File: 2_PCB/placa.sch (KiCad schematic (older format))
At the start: 35 parts

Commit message: Updated some sensor values; Finished choice of components; Placements of components in PCB
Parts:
- removed C? (x2): 100n, symbol Device:C
- added C13: 660n, Capacitor_SMD:C_0805_2012Metric_Pad1.15x1.40mm_HandSolder, symbol Device:C
- added C15: 100n, Capacitor_SMD:C_0805_2012Metric_Pad1.15x1.40mm_HandSolder, symbol Device:C
- added C16: 470n, Capacitor_SMD:C_0805_2012Metric_Pad1.15x1.40mm_HandSolder, symbol Device:C
- added J1: Screw_Terminal_01x02, Connector_PinHeader_2.54mm:PinHeader_1x02_P2.54mm_Vertical, symbol Connector:Screw_Terminal_01x02
- added JP1: SolderJumper_3_Bridged12, Jumper:SolderJumper-3_P1.3mm_Bridged12_RoundedPad1.0x1.5mm_NumberLabels, symbol Jumper:SolderJumper_3_Bridged12
- C1, C3, C8: renamed from C?; footprint (none) -> Capacitor_SMD:C_0805_2012Metric_Pad1.15x1.40mm_HandSolder
- C10: renamed from C?; value CP1 -> 660n; footprint (none) -> Capacitor_SMD:C_0805_2012Metric_Pad1.15x1.40mm_HandSolder
- C11, C14: renamed from C?; value C_Small -> 10p; footprint (none) -> Capacitor_SMD:C_0805_2012Metric_Pad1.15x1.40mm_HandSolder
- C2: renamed from C?; value C -> 100n; footprint (none) -> Capacitor_SMD:C_0805_2012Metric_Pad1.15x1.40mm_HandSolder
- C4: renamed from C?; value CP1 -> 10u; footprint (none) -> Capacitor_THT:CP_Radial_D5.0mm_P2.50mm
- C5: renamed from C?; value CP1 -> 1u; footprint (none) -> Capacitor_THT:CP_Radial_D5.0mm_P2.00mm
- C6, C9: renamed from C?; value C_Small -> 20p; footprint (none) -> Capacitor_SMD:C_0805_2012Metric_Pad1.15x1.40mm_HandSolder
- C7: renamed from C?; value 100n -> 660n; footprint (none) -> Capacitor_SMD:C_0805_2012Metric_Pad1.15x1.40mm_HandSolder
- D1, D2: renamed from D?; footprint (none) -> LED_SMD:LED_0805_2012Metric_Pad1.15x1.40mm_HandSolder
- J2: renamed from J?; footprint (none) -> Connector_PinHeader_2.54mm:PinHeader_1x05_P2.54mm_Vertical
- J3: renamed from J?; footprint (none) -> Connector_PinHeader_2.54mm:PinHeader_1x02_P2.54mm_Vertical
- R1, R10, R4, R6, R9: renamed from R?; footprint (none) -> Resistor_SMD:R_0805_2012Metric_Pad1.15x1.40mm_HandSolder
- R2, R3: renamed from R?; value R -> 330; footprint (none) -> Resistor_SMD:R_0805_2012Metric_Pad1.15x1.40mm_HandSolder
- R5: renamed from R?; value R -> 390; footprint (none) -> Resistor_SMD:R_0805_2012Metric_Pad1.15x1.40mm_HandSolder
- R7: renamed from R?; value R -> 10k; footprint (none) -> Resistor_SMD:R_0805_2012Metric_Pad1.15x1.40mm_HandSolder
- R8: renamed from R?; value R_Variable -> HR202; footprint (none) -> Resistor_THT:R_Box_L8.4mm_W2.5mm_P5.08mm
- SW1: renamed from SW?; footprint (none) -> TCC:BUTTON_5mm
- TH1: renamed from TH?; footprint (none) -> Resistor_THT:R_Axial_DIN0204_L3.6mm_D1.6mm_P1.90mm_Vertical
- Y1: renamed from Y?; value Crystal_Small -> 8 MHz; footprint (none) -> Crystal:Crystal_HC49-U_Vertical
- Y2: renamed from Y?; value Crystal_Small -> 32.768 kHz; footprint (none) -> Crystal:Crystal_Round_D1.0mm_Vertical
- gave numbers to parts that had none: 3
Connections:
- net labels added: PWR_MS, PWR_RH, PWR_TEMP, UART_RX, UART_TX
- net labels removed: VDDA
- wire segments 156 -> 177
- no-connect marks 8 -> 24
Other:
- note added: "LoRa RA-01"
- note added: "Microcontroller"
- note added: "UART Connection"
- moved on the sheet: C11, C14, C2, C3, C4, C6, C7, C9, D1, D2, R1, R2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

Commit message: Remap SPI pins, reposition components; start routing
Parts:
- added J4: TestPoints, Connector_PinHeader_2.54mm:PinHeader_1x04_P2.54mm_Vertical, symbol Connector:Conn_01x04_Female
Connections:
- wire segments 177 -> 181
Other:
- moved on the sheet: C16, C3, C4
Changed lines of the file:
@@
 Text Notes 6000 650  0    50   ~ 0
 Power Supply
-Wire Notes Line
-	5650 1900 11200 1900
 $Comp
 L Connector:Conn_01x05_Male J2
@@
 Wire Wire Line
 	3650 4800 3450 4800
-Text Label 1300 7200 0    50   ~ 0
+Text Label 1300 7300 0    50   ~ 0
 SWCLK
 Text Label 1300 7100 0    50   ~ 0
 SWDIO
-Text Label 1300 7300 0    50   ~ 0
+Text Label 1300 7200 0    50   ~ 0
 NRST
 $Comp
@@
 NoConn ~ 7600 3400
 NoConn ~ 6600 2800
-Wire Wire Line
-	3450 4000 3650 4000
-Wire Wire Line
-	3450 4100 3650 4100
-Wire Wire Line
-	3450 4200 3650 4200
-Text Label 3650 4000 0    50   ~ 0
+Text Label 2150 3800 2    50   ~ 0
 SPI_SCK
-Text Label 3650 4100 0    50   ~ 0
+Text Label 2150 3900 2    50   ~ 0
 SPI_MISO
-Text Label 3650 4200 0    50   ~ 0
+Text Label 2150 4000 2    50   ~ 0
 SPI_MOSI
 Text Label 6450 3300 2    50   ~ 0
@@
 Text Label 6450 3500 2    50   ~ 0
 SPI_MOSI
-Wire Wire Line
-	6450 3300 6600 3300
-Wire Wire Line
-	6450 3500 6600 3500
 Wire Wire Line
 	6000 3400 6600 3400
@@
 	1    0    0    -1
 $EndComp
-Wire Wire Line
-	6600 3200 6450 3200
 Text Label 6450 3200 2    50   ~ 0
 SPI_CS
-Text Label 2150 3500 2    50   ~ 0
+Text Label 2150 4100 2    50   ~ 0
 SPI_CS
-Wire Wire Line
-	2150 3500 2250 3500
-Wire Wire Line
-	2250 3600 2150 3600
-Text Label 2150 3600 2    50   ~ 0
+Text Label 2150 3100 2    50   ~ 0
 LoRa_Reset
 Text Label 6450 3000 2    50   ~ 0
@@
 Wire Wire Line
 	3450 3500 3650 3500
+Text Label 3650 3500 0    50   ~ 0
+ADC_RH
+Wire Wire Line
+	3450 3700 3650 3700
 Text Label 3650 3700 0    50   ~ 0
-ADC_RH
-Wire Wire Line
-	3450 3700 3650 3700
-Text Label 3650 3500 0    50   ~ 0
 ADC_TEMP
 Text Label 10500 4350 0    50   ~ 0
@@
 L power:GND #PWR0121
 U 1 1 5B9632C9
-P 3800 2800
-F 0 "#PWR0121" H 3800 2550 50  0001 C CNN
-F 1 "GND" H 3805 2627 50  0000 C CNN
-F 2 "" H 3800 2800 50  0001 C CNN
-F 3 "" H 3800 2800 50  0001 C CNN
-	1    3800 2800
+P 3700 2800
+F 0 "#PWR0121" H 3700 2550 50  0001 C CNN
+F 1 "GND" H 3705 2627 50  0000 C CNN
+F 2 "" H 3700 2800 50  0001 C CNN
+F 3 "" H 3700 2800 50  0001 C CNN
+	1    3700 2800
 	1    0    0    -1
 $EndComp
@@
 L power:VCC #PWR0122
 U 1 1 5B963B24
-P 3800 2300
-F 0 "#PWR0122" H 3800 2150 50  0001 C CNN
-F 1 "VCC" H 3817 2473 50  0000 C CNN
-F 2 "" H 3800 2300 50  0001 C CNN
-F 3 "" H 3800 2300 50  0001 C CNN
-	1    3800 2300
+P 3700 2300
+F 0 "#PWR0122" H 3700 2150 50  0001 C CNN
+F 1 "VCC" H 3717 2473 50  0000 C CNN
+F 2 "" H 3700 2300 50  0001 C CNN
+F 3 "" H 3700 2300 50  0001 C CNN
+	1    3700 2300
 	1    0    0    -1
 $EndComp
@@
 L Device:C C3
 U 1 1 5B9646E9
-P 4050 2550
-F 0 "C3" H 4165 2596 50  0000 L CNN
-F 1 "100n" H 4165 2505 50  0000 L CNN
-F 2 "Capacitor_SMD:C_0805_2012Metric_Pad1.15x1.40mm_HandSolder" H 4088 2400 50  0001 C CNN
-F 3 "~" H 4050 2550 50  0001 C CNN
-	1    4050 2550
-	1    0    0    -1
-$EndComp
-Wire Wire Line
-	3800 2300 3800 2350
-Wire Wire Line
-	3800 2800 3800 2750
-Wire Wire Line
-	3800 2750 4050 2750
-Wire Wire Line
-	4050 2750 4050 2700
-Wire Wire Line
-	4050 2350 4050 2400
-Wire Wire Line
-	3800 2350 4050 2350
+P 3950 2550
+F 0 "C3" H 4065 2596 50  0000 L CNN
+F 1 "100n" H 4065 2505 50  0000 L CNN
+F 2 "Capacitor_SMD:C_0805_2012Metric_Pad1.15x1.40mm_HandSolder" H 3988 2400 50  0001 C CNN
+F 3 "~" H 3950 2550 50  0001 C CNN
+	1    3950 2550
+	1    0    0    -1
+$EndComp
+Wire Wire Line
+	3700 2300 3700 2350
+Wire Wire Line
+	3700 2800 3700 2750
+Wire Wire Line
+	3700 2750 3950 2750
+Wire Wire Line
+	3950 2750 3950 2700
+Wire Wire Line
+	3950 2350 3950 2400
+Wire Wire Line
+	3700 2350 3950 2350
 $Comp
 L Device:CP1 C4
 U 1 1 5B97312D
-P 4550 2550
-F 0 "C4" H 4665 2596 50  0000 L CNN
-F 1 "10u" H 4665 2505 50  0000 L CNN
-F 2 "Capacitor_THT:CP_Radial_D5.0mm_P2.50mm" H 4550 2550 50  0001 C CNN
-F 3 "~" H 4550 2550 50  0001 C CNN
-	1    4550 2550
-	1    0    0    -1
-$EndComp
-Wire Wire Line
-	4550 2400 4550 2350
-Wire Wire Line
-	4550 2350 4050 2350
-Connection ~ 4050 2350
-Wire Wire Line
-	4550 2700 4550 2750
-Wire Wire Line
-	4550 2750 4050 2750
-Connection ~ 4050 2750
+P 4450 2550
+F 0 "C4" H 4565 2596 50  0000 L CNN
+F 1 "10u" H 4565 2505 50  0000 L CNN
+F 2 "Capacitor_THT:CP_Radial_D5.0mm_P2.50mm" H 4450 2550 50  0001 C CNN
+F 3 "~" H 4450 2550 50  0001 C CNN
+	1    4450 2550
+	1    0    0    -1
+$EndComp
+Wire Wire Line
+	4450 2400 4450 2350
+Wire Wire Line
+	4450 2350 3950 2350
+Connection ~ 3950 2350
+Wire Wire Line
+	4450 2700 4450 2750
+Wire Wire Line
+	4450 2750 3950 2750
+Connection ~ 3950 2750
 Wire Wire Line
 	8350 5900 8350 5450
@@
 Text Label 9000 3600 2    50   ~ 0
 PWR_RH
-Text Label 2150 3700 2    50   ~ 0
+Text Label 3650 4000 0    50   ~ 0
 PWR_RH
 Text Label 3650 3800 0    50   ~ 0
@@
 Wire Wire Line
 	3450 3900 3650 3900
-Wire Wire Line
-	2150 3700 2250 3700
 Text Notes 5800 2100 0    50   ~ 0
 LoRa RA-01
-Wire Notes Line
-	5650 4850 8450 4850
 Wire Wire Line
 	2950 1950 3050 1950
@@
 Microcontroller
 Wire Notes Line
-	5650 500  5650 4850
+	5200 500  5200 4850
 Wire Wire Line
 	3650 4500 3450 4500
@@
 NoConn ~ 2250 4500
 NoConn ~ 2250 4400
-NoConn ~ 2250 4300
-NoConn ~ 2250 4200
-NoConn ~ 2250 4100
-NoConn ~ 2250 4000
-NoConn ~ 2250 3900
-NoConn ~ 2250 3800
 $Comp
 L power:VCC #PWR0106
@@
 	1    0    0    -1
 $EndComp
-NoConn ~ 2250 3100
 Wire Wire Line
 	1600 2400 2250 2400
@@
 L Device:C C16
 U 1 1 5BA91F5E
-P 4900 2550
-F 0 "C16" H 5015 2596 50  0000 L CNN
-F 1 "470n" H 5015 2505 50  0000 L CNN
-F 2 "Capacitor_SMD:C_0805_2012Metric_Pad1.15x1.40mm_HandSolder" H 4938 2400 50  0001 C CNN
-F 3 "~" H 4900 2550 50  0001 C CNN
-	1    4900 2550
-	1    0    0    -1
-$EndComp
-Wire Wire Line
-	4550 2350 4900 2350
-Wire Wire Line
-	4900 2350 4900 2400
-Connection ~ 4550 2350
-Wire Wire Line
-	4900 2700 4900 2750
-Wire Wire Line
-	4900 2750 4550 2750
-Connection ~ 4550 2750
+P 4800 2550
+F 0 "C16" H 4915 2596 50  0000 L CNN
+F 1 "470n" H 4915 2505 50  0000 L CNN
+F 2 "Capacitor_SMD:C_0805_2012Metric_Pad1.15x1.40mm_HandSolder" H 4838 2400 50  0001 C CNN
+F 3 "~" H 4800 2550 50  0001 C CNN
+	1    4800 2550
+	1    0    0    -1
+$EndComp
+Wire Wire Line
+	4450 2350 4800 2350
+Wire Wire Line
+	4800 2350 4800 2400
+Connection ~ 4450 2350
+Wire Wire Line
+	4800 2700 4800 2750
+Wire Wire Line
+	4800 2750 4450 2750
+Connection ~ 4450 2750
 $Comp
 L power:VCC #PWR0126
@@
 	0    -1   -1   0
 $EndComp
+Wire Wire Line
+	2150 3800 2250 3800
+Wire Wire Line
+	2250 3900 2150 3900
+Wire Wire Line
+	2150 4000 2250 4000
+NoConn ~ 3450 4100
+NoConn ~ 3450 4200
+NoConn ~ 2250 4200
+NoConn ~ 2250 3500
+NoConn ~ 2250 3600
+Wire Wire Line
+	2150 4100 2250 4100
+Wire Notes Line
+	5200 1900 11200 1900
+Wire Notes Line
+	5200 4850 8450 4850
+$Comp
+L Connector:Conn_01x04_Female J4
+U 1 1 5BA72F71
+P 5400 4550
+F 0 "J4" H 5294 4835 50  0000 C CNN
+F 1 "TestPoints" H 5294 4744 50  0000 C CNN
+F 2 "Connector_PinHeader_2.54mm:PinHeader_1x04_P2.54mm_Vertical" H 5400 4550 50  0001 C CNN
+F 3 "~" H 5400 4550 50  0001 C CNN
+	1    5400 4550
+	-1   0    0    -1
+$EndComp
+Wire Wire Line
+	6450 3500 6600 3500
+Text Label 5750 4550 0    50   ~ 0
+SPI_MOSI
+Wire Wire Line
+	2150 3100 2250 3100
+NoConn ~ 2250 4300
+Wire Wire Line
+	6450 3300 6600 3300
+Wire Wire Line
+	6600 3200 6450 3200
+Text Label 5750 4450 0    50   ~ 0
+SPI_CS
+Text Label 5750 4650 0    50   ~ 0
+SPI_MISO
+Text Label 5750 4750 0    50   ~ 0
+SPI_SCK
+Wire Wire Line
+	5600 4750 5750 4750
+Wire Wire Line
+	5600 4650 5750 4650
+Wire Wire Line
+	5750 4550 5600 4550
+Wire Wire Line
+	5600 4450 5750 4450
+Wire Wire Line
+	3450 4000 3650 4000
+NoConn ~ 2250 3700
 $EndSCHEMATC

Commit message: Finished first iteration of PCB
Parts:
- U2: footprint RF_Module:Ai-Thinker-Ra-01-LoRa -> TCC:Ai-Thinker-Ra-01-LoRa
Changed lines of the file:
@@
 F 0 "U2" H 7350 4050 50  0000 C CNN
 F 1 "Ai-Thinker-Ra-01" H 6650 4050 50  0000 C CNN
-F 2 "RF_Module:Ai-Thinker-Ra-01-LoRa" H 8100 2900 50  0001 C CNN
+F 2 "TCC:Ai-Thinker-Ra-01-LoRa" H 8100 2900 50  0001 C CNN
 F 3 "https://mikroelectron.com/Product/10KM-433M-LORA-LONG-RANGE-WIRELESS-MODULE-RA-01" H 7200 4000 50  0001 C CNN
 	1    7100 3300
@@
 Wire Wire Line
 	6450 3000 6600 3000
-Wire Wire Line
-	3450 4600 3650 4600
-Text Label 3650 4600 0    50   ~ 0
+Text Label 2150 4700 2    50   ~ 0
 userLED
 Text Label 5100 6850 0    50   ~ 0
@@
 NoConn ~ 2250 4900
 NoConn ~ 2250 4800
-NoConn ~ 2250 4700
 NoConn ~ 2250 4600
 NoConn ~ 2250 4500
@@
 	3450 4000 3650 4000
 NoConn ~ 2250 3700
+NoConn ~ 3450 4600
+Wire Wire Line
+	2250 4700 2150 4700
 $EndSCHEMATC

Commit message: Created and added capacitive sensor to PCB; Minor changes to the design
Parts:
- C12: footprint (none) -> TCC:Moisture Sensor
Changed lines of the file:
@@
 F 0 "C12" H 9915 1346 50  0000 L CNN
 F 1 "C_Variable" H 9915 1255 50  0000 L CNN
-F 2 "" H 9800 1300 50  0001 C CNN
+F 2 "TCC:Moisture Sensor" H 9800 1300 50  0001 C CNN
 F 3 "~" H 9800 1300 50  0001 C CNN
 	1    9800 1300

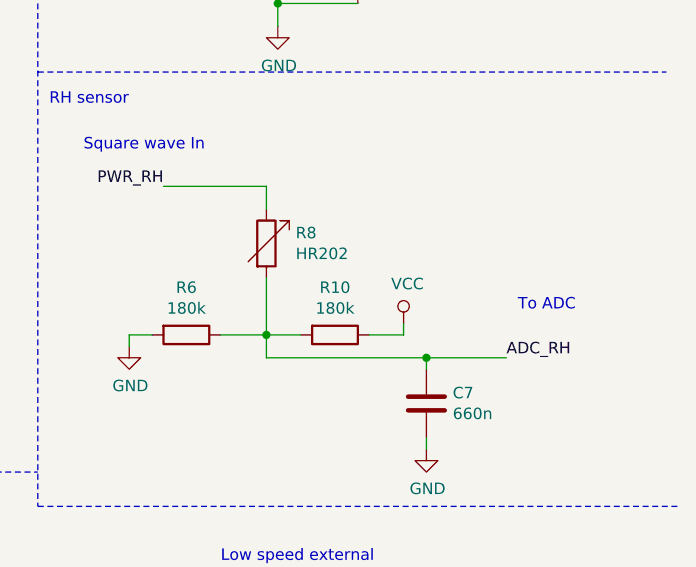
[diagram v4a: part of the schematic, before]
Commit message: Got LaTeX doc working according to ABNT. Uploaded simulation files of the moisture sensor capacitor. Small changes to the board
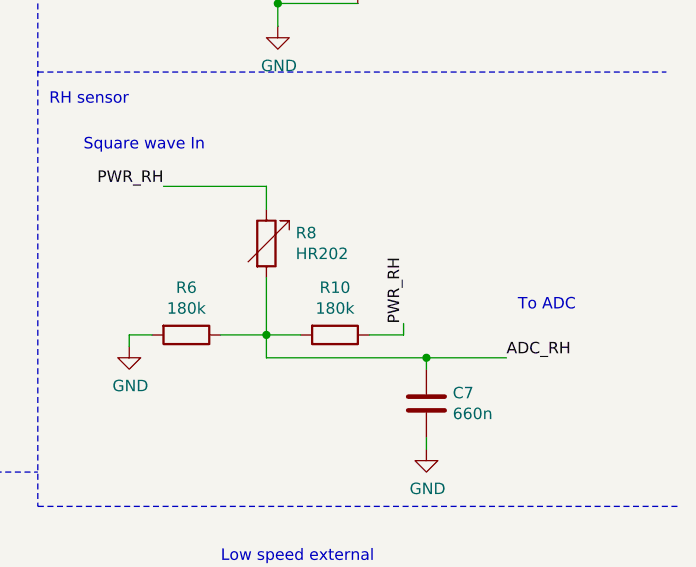
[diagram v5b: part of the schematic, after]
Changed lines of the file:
@@
 NoConn ~ 2250 4500
 NoConn ~ 2250 4400
-$Comp
-L power:VCC #PWR0106
-U 1 1 5BA61988
-P 10050 4200
-F 0 "#PWR0106" H 10050 4050 50  0001 C CNN
-F 1 "VCC" H 10067 4373 50  0000 C CNN
-F 2 "" H 10050 4200 50  0001 C CNN
-F 3 "" H 10050 4200 50  0001 C CNN
-	1    10050 4200
-	1    0    0    -1
-$EndComp
 Wire Wire Line
 	1600 2400 2250 2400
@@
 Wire Wire Line
 	2250 4700 2150 4700
+Text Label 10050 4200 1    50   ~ 0
+PWR_RH
 $EndSCHEMATC

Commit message: PCB version 1.1: Easier to home etch and added a BOOT0 PD resistor
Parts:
- removed J2: Conn_01x05_Male, Connector_PinHeader_2.54mm:PinHeader_1x05_P2.54mm_Vertical, symbol Connector:Conn_01x05_Male
- removed JP1: SolderJumper_3_Bridged12, Jumper:SolderJumper-3_P1.3mm_Bridged12_RoundedPad1.0x1.5mm_NumberLabels, symbol Jumper:SolderJumper_3_Bridged12
- removed SW1: SW_Push, TCC:BUTTON_5mm, symbol Switch:SW_Push
- added J2: Conn_01x04_Male, Connector_PinHeader_2.54mm:PinHeader_1x04_P2.54mm_Vertical, symbol Connector:Conn_01x04_Male
- added J5: Conn_01x02_Male, Connector_PinHeader_2.54mm:PinHeader_1x02_P2.54mm_Vertical, symbol Connector:Conn_01x02_Male
- added R11: 10k, Resistor_SMD:R_0805_2012Metric_Pad1.15x1.40mm_HandSolder, symbol Device:R
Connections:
- wire segments 181 -> 174
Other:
- moved on the sheet: C1
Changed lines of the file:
@@
 Text Notes 6000 650  0    50   ~ 0
 Power Supply
-$Comp
-L Connector:Conn_01x05_Male J2
-U 1 1 5B8D4541
-P 900 7200
-F 0 "J2" H 1006 7578 50  0000 C CNN
-F 1 "Conn_01x05_Male" H 1006 7487 50  0000 C CNN
-F 2 "Connector_PinHeader_2.54mm:PinHeader_1x05_P2.54mm_Vertical" H 900 7200 50  0001 C CNN
-F 3 "~" H 900 7200 50  0001 C CNN
-	1    900  7200
-	1    0    0    -1
-$EndComp
 Text Notes 550  6450 0    50   ~ 0
 ST-Link connection
@@
 L power:GND #PWR0109
 U 1 1 5B8D5FED
-P 1250 7450
-F 0 "#PWR0109" H 1250 7200 50  0001 C CNN
-F 1 "GND" H 1255 7277 50  0000 C CNN
-F 2 "" H 1250 7450 50  0001 C CNN
-F 3 "" H 1250 7450 50  0001 C CNN
-	1    1250 7450
-	1    0    0    -1
-$EndComp
-Wire Wire Line
-	1100 7400 1250 7400
-Wire Wire Line
-	1250 7400 1250 7450
+P 1450 7650
+F 0 "#PWR0109" H 1450 7400 50  0001 C CNN
+F 1 "GND" H 1455 7477 50  0000 C CNN
+F 2 "" H 1450 7650 50  0001 C CNN
+F 3 "" H 1450 7650 50  0001 C CNN
+	1    1450 7650
+	1    0    0    -1
+$EndComp
 Text Label 2100 2200 2    50   ~ 0
 NRST
@@
 Wire Wire Line
 	3650 4800 3450 4800
-Text Label 1300 7300 0    50   ~ 0
+Text Label 900  7000 0    50   ~ 0
 SWCLK
-Text Label 1300 7100 0    50   ~ 0
+Text Label 900  7300 0    50   ~ 0
 SWDIO
-Text Label 1300 7200 0    50   ~ 0
+Text Label 1000 7550 0    50   ~ 0
 NRST
 $Comp
 L power:VCC #PWR0110
 U 1 1 5B8DD502
-P 1400 6950
-F 0 "#PWR0110" H 1400 6800 50  0001 C CNN
-F 1 "VCC" H 1417 7123 50  0000 C CNN
-F 2 "" H 1400 6950 50  0001 C CNN
-F 3 "" H 1400 6950 50  0001 C CNN
-	1    1400 6950
-	1    0    0    -1
-$EndComp
-Wire Wire Line
-	1300 7300 1100 7300
-Wire Wire Line
-	1100 7200 1300 7200
-Wire Wire Line
-	1300 7100 1100 7100
-Wire Wire Line
-	1100 7000 1400 7000
-Wire Wire Line
-	1400 7000 1400 6950
-Wire Wire Line
-	1250 7400 1750 7400
-Connection ~ 1250 7400
-Wire Wire Line
-	1750 7000 1400 7000
-Connection ~ 1400 7000
+P 1450 7200
+F 0 "#PWR0110" H 1450 7050 50  0001 C CNN
+F 1 "VCC" H 1467 7373 50  0000 C CNN
+F 2 "" H 1450 7200 50  0001 C CNN
+F 3 "" H 1450 7200 50  0001 C CNN
+	1    1450 7200
+	1    0    0    -1
+$EndComp
 $Comp
 L Device:C C1
 U 1 1 5B8E21D1
-P 1750 7200
-F 0 "C1" H 1865 7246 50  0000 L CNN
-F 1 "100n" H 1865 7155 50  0000 L CNN
-F 2 "Capacitor_SMD:C_0805_2012Metric_Pad1.15x1.40mm_HandSolder" H 1788 7050 50  0001 C CNN
-F 3 "~" H 1750 7200 50  0001 C CNN
-	1    1750 7200
-	1    0    0    -1
-$EndComp
-Wire Wire Line
-	1750 7050 1750 7000
-Wire Wire Line
-	1750 7350 1750 7400
+P 1450 7450
+F 0 "C1" H 1565 7496 50  0000 L CNN
+F 1 "100n" H 1565 7405 50  0000 L CNN
+F 2 "Capacitor_SMD:C_0805_2012Metric_Pad1.15x1.40mm_HandSolder" H 1488 7300 50  0001 C CNN
+F 3 "~" H 1450 7450 50  0001 C CNN
+	1    1450 7450
+	1    0    0    -1
+$EndComp
 $Comp
 L power:VCC #PWR0111
@@
 	3000 6950 3250 6950
 Connection ~ 3000 6950
-$Comp
-L Switch:SW_Push SW1
-U 1 1 5B8EAC92
-P 2450 7250
-F 0 "SW1" V 2496 7202 50  0000 R CNN
-F 1 "SW_Push" V 2405 7202 50  0000 R CNN
-F 2 "TCC:BUTTON_5mm" H 2450 7450 50  0001 C CNN
-F 3 "" H 2450 7450 50  0001 C CNN
-	1    2450 7250
-	0    -1   -1   0
-$EndComp
-Wire Wire Line
-	2450 7450 2450 7500
-Wire Wire Line
-	2450 7500 3000 7500
-Wire Wire Line
-	3000 7500 3000 7350
-Wire Wire Line
-	3000 7500 3000 7600
-Connection ~ 3000 7500
 $Comp
 L power:GND #PWR0112
@@
 Wire Wire Line
 	3000 6950 3000 7050
-Wire Wire Line
-	2450 6950 3000 6950
-Wire Wire Line
-	2450 6950 2450 7050
 Text Label 3650 4400 0    50   ~ 0
 UART_TX
@@
 	3450 4400 3650 4400
 $Comp
-L power:VCC #PWR0124
-U 1 1 5B98FB2B
-P 1450 2150
-F 0 "#PWR0124" H 1450 2000 50  0001 C CNN
-F 1 "VCC" H 1467 2323 50  0000 C CNN
-F 2 "" H 1450 2150 50  0001 C CNN
-F 3 "" H 1450 2150 50  0001 C CNN
-	1    1450 2150
-	1    0    0    -1
-$EndComp
-Wire Wire Line
-	1450 2150 1450 2200
-Wire Wire Line
-	1450 2600 1450 2700
-$Comp
 L power:GND #PWR0125
 U 1 1 5B99E910
@@
 NoConn ~ 2250 4500
 NoConn ~ 2250 4400
-Wire Wire Line
-	1600 2400 2250 2400
 $Comp
 L Device:C C16
@@
 	1    7800 2700
 	1    0    0    -1
-$EndComp
-$Comp
-L Jumper:SolderJumper_3_Bridged12 JP1
-U 1 1 5B9CA536
-P 1450 2400
-F 0 "JP1" H 1400 2500 50  0000 L CNN
-F 1 "SolderJumper_3_Bridged12" H 900 2700 50  0000 L CNN
-F 2 "Jumper:SolderJumper-3_P1.3mm_Bridged12_RoundedPad1.0x1.5mm_NumberLabels" H 1450 2400 50  0001 C CNN
-F 3 "~" H 1450 2400 50  0001 C CNN
-	1    1450 2400
-	0    -1   -1   0
 $EndComp
 Wire Wire Line
@@
 Text Label 10050 4200 1    50   ~ 0
 PWR_RH
+$Comp
+L Device:R R11
+U 1 1 5BB41864
+P 1850 2400
+F 0 "R11" H 1920 2446 50  0000 L CNN
+F 1 "10k" H 1920 2355 50  0000 L CNN
+F 2 "Resistor_SMD:R_0805_2012Metric_Pad1.15x1.40mm_HandSolder" V 1780 2400 50  0001 C CNN
+F 3 "~" H 1850 2400 50  0001 C CNN
+	1    1850 2400
+	0    1    1    0
+$EndComp
+Wire Wire Line
+	2000 2400 2250 2400
+Wire Wire Line
+	1450 2400 1450 2700
+Wire Wire Line
+	1450 2400 1700 2400
+$Comp
+L Connector:Conn_01x04_Male J2
+U 1 1 5BB700CF
+P 650 7100
+F 0 "J2" H 756 7378 50  0000 C CNN
+F 1 "Conn_01x04_Male" H 756 7287 50  0000 C CNN
+F 2 "Connector_PinHeader_2.54mm:PinHeader_1x04_P2.54mm_Vertical" H 650 7100 50  0001 C CNN
+F 3 "~" H 650 7100 50  0001 C CNN
+	1    650  7100
+	1    0    0    -1
+$EndComp
+$Comp
+L power:GND #PWR0106
+U 1 1 5BB95E51
+P 950 7100
+F 0 "#PWR0106" H 950 6850 50  0001 C CNN
+F 1 "GND" H 955 6927 50  0000 C CNN
+F 2 "" H 950 7100 50  0001 C CNN
+F 3 "" H 950 7100 50  0001 C CNN
+	1    950  7100
+	0    -1   -1   0
+$EndComp
+Wire Wire Line
+	900  7300 850  7300
+Wire Wire Line
+	900  7000 850  7000
+Wire Wire Line
+	1450 7650 1450 7600
+Wire Wire Line
+	3000 7350 3000 7600
+$Comp
+L Connector:Conn_01x02_Male J5
+U 1 1 5BBE81FC
+P 600 7550
+F 0 "J5" H 706 7728 50  0000 C CNN
+F 1 "Conn_01x02_Male" H 706 7637 50  0000 C CNN
+F 2 "Connector_PinHeader_2.54mm:PinHeader_1x02_P2.54mm_Vertical" H 600 7550 50  0001 C CNN
+F 3 "~" H 600 7550 50  0001 C CNN
+	1    600  7550
+	1    0    0    -1
+$EndComp
+$Comp
+L power:GND #PWR0124
+U 1 1 5BBF1F50
+P 900 7700
+F 0 "#PWR0124" H 900 7450 50  0001 C CNN
+F 1 "GND" H 905 7527 50  0000 C CNN
+F 2 "" H 900 7700 50  0001 C CNN
+F 3 "" H 900 7700 50  0001 C CNN
+	1    900  7700
+	1    0    0    -1
+$EndComp
+Wire Wire Line
+	800  7550 1000 7550
+Wire Wire Line
+	800  7650 900  7650
+Wire Wire Line
+	900  7650 900  7700
+Wire Wire Line
+	1450 7200 1450 7300
+Wire Wire Line
+	850  7200 1450 7200
+Connection ~ 1450 7200
+Wire Wire Line
+	950  7100 850  7100
 $EndSCHEMATC
